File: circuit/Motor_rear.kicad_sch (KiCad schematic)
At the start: 42 parts, among them J15 motor1, J16 motor1, Q13 DMHT6016LFJ, Q14 DMHT6016LFJ, Q19 DMN1054UCB4, Q20 DMN1054UCB4, U13 SN74LVC1G18DSFR, U14 SN74LVC1G18DSFR, U15 DRV8701, U16 DRV8701

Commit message: AD変換の取得ができた
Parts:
- Q13, Q14: symbol robocon:DMHT6016LFJ -> robot_contest:DMHT6016LFJ
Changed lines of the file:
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@@
 	)
 	(symbol
-		(lib_id "robocon:DMHT6016LFJ")
+		(lib_id "robot_contest:DMHT6016LFJ")
 		(at 209.55 55.88 90)
 		(unit 1)
@@
 	)
 	(symbol
-		(lib_name "DMHT6016LFJ_1")
-		(lib_id "robocon:DMHT6016LFJ")
+		(lib_id "robot_contest:DMHT6016LFJ")
 		(at 209.55 133.35 90)
 		(unit 1)

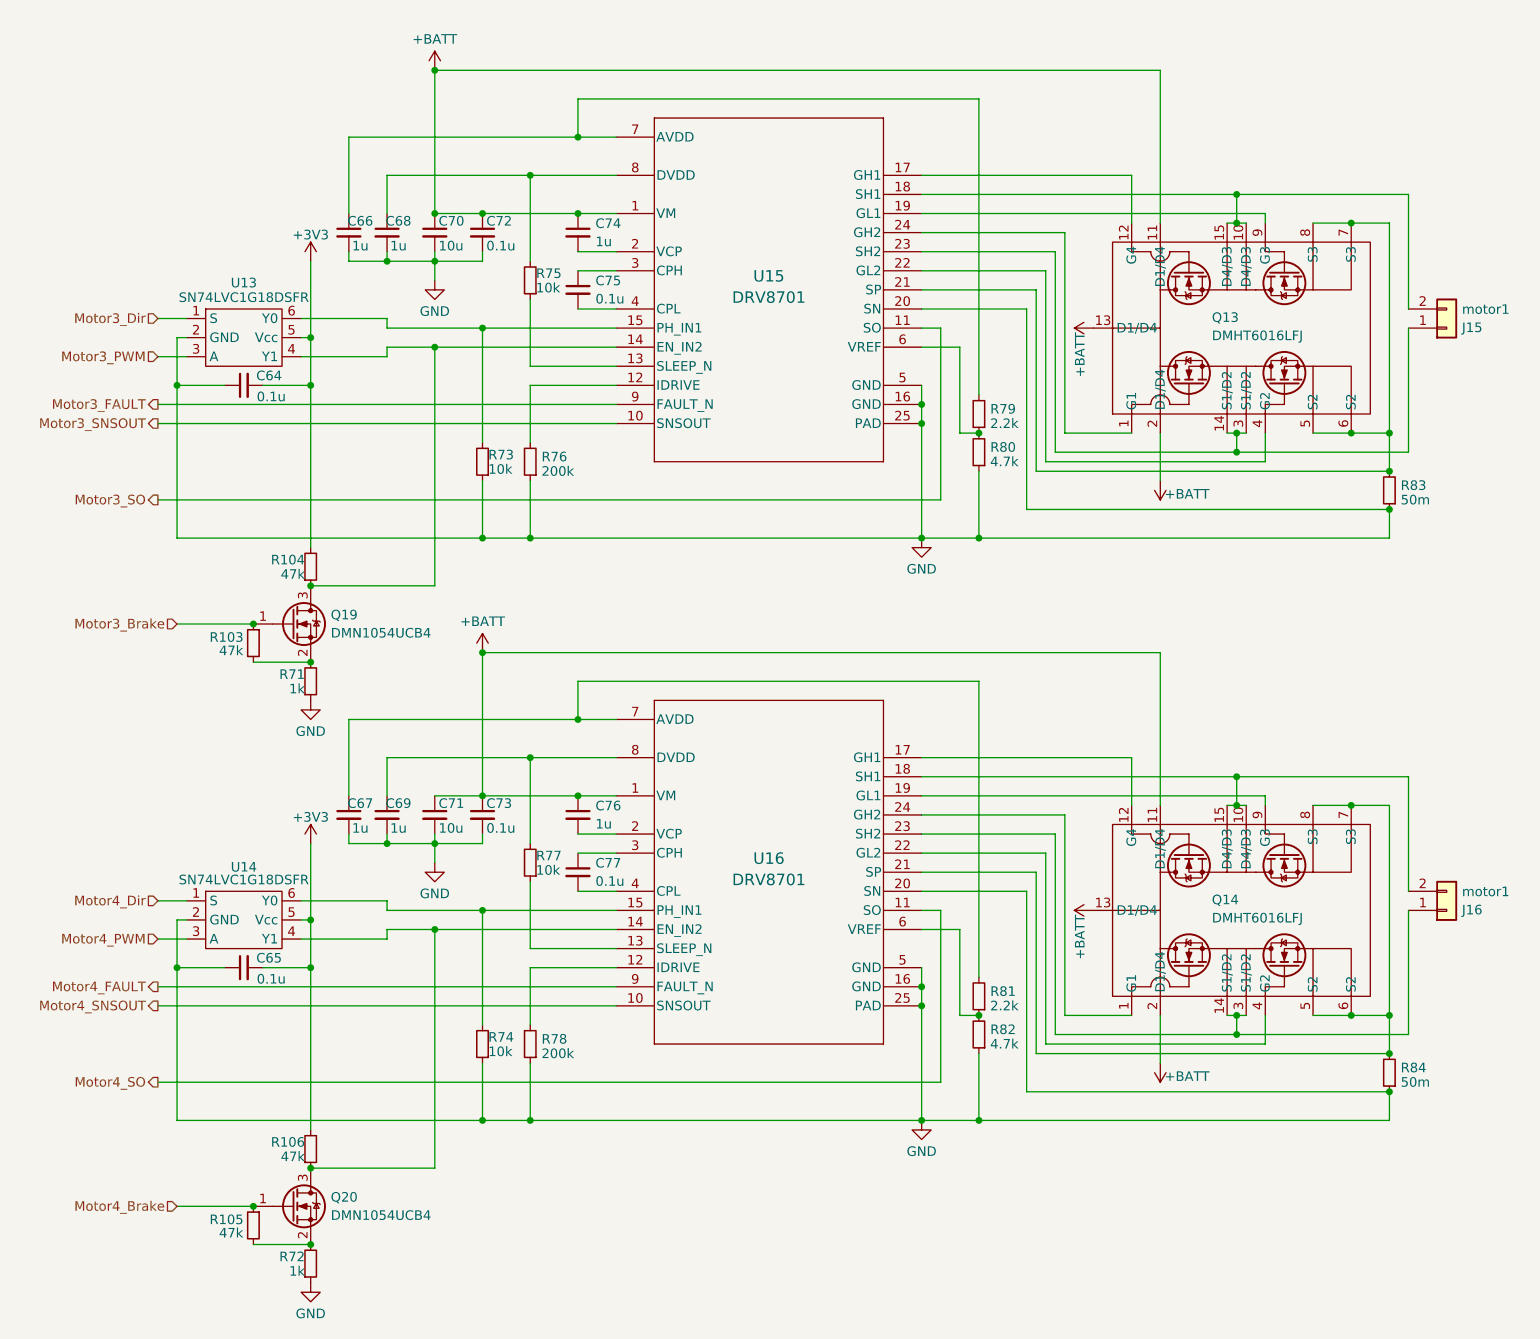
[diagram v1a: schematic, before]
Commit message: スマコンの設定変更 回路図変更
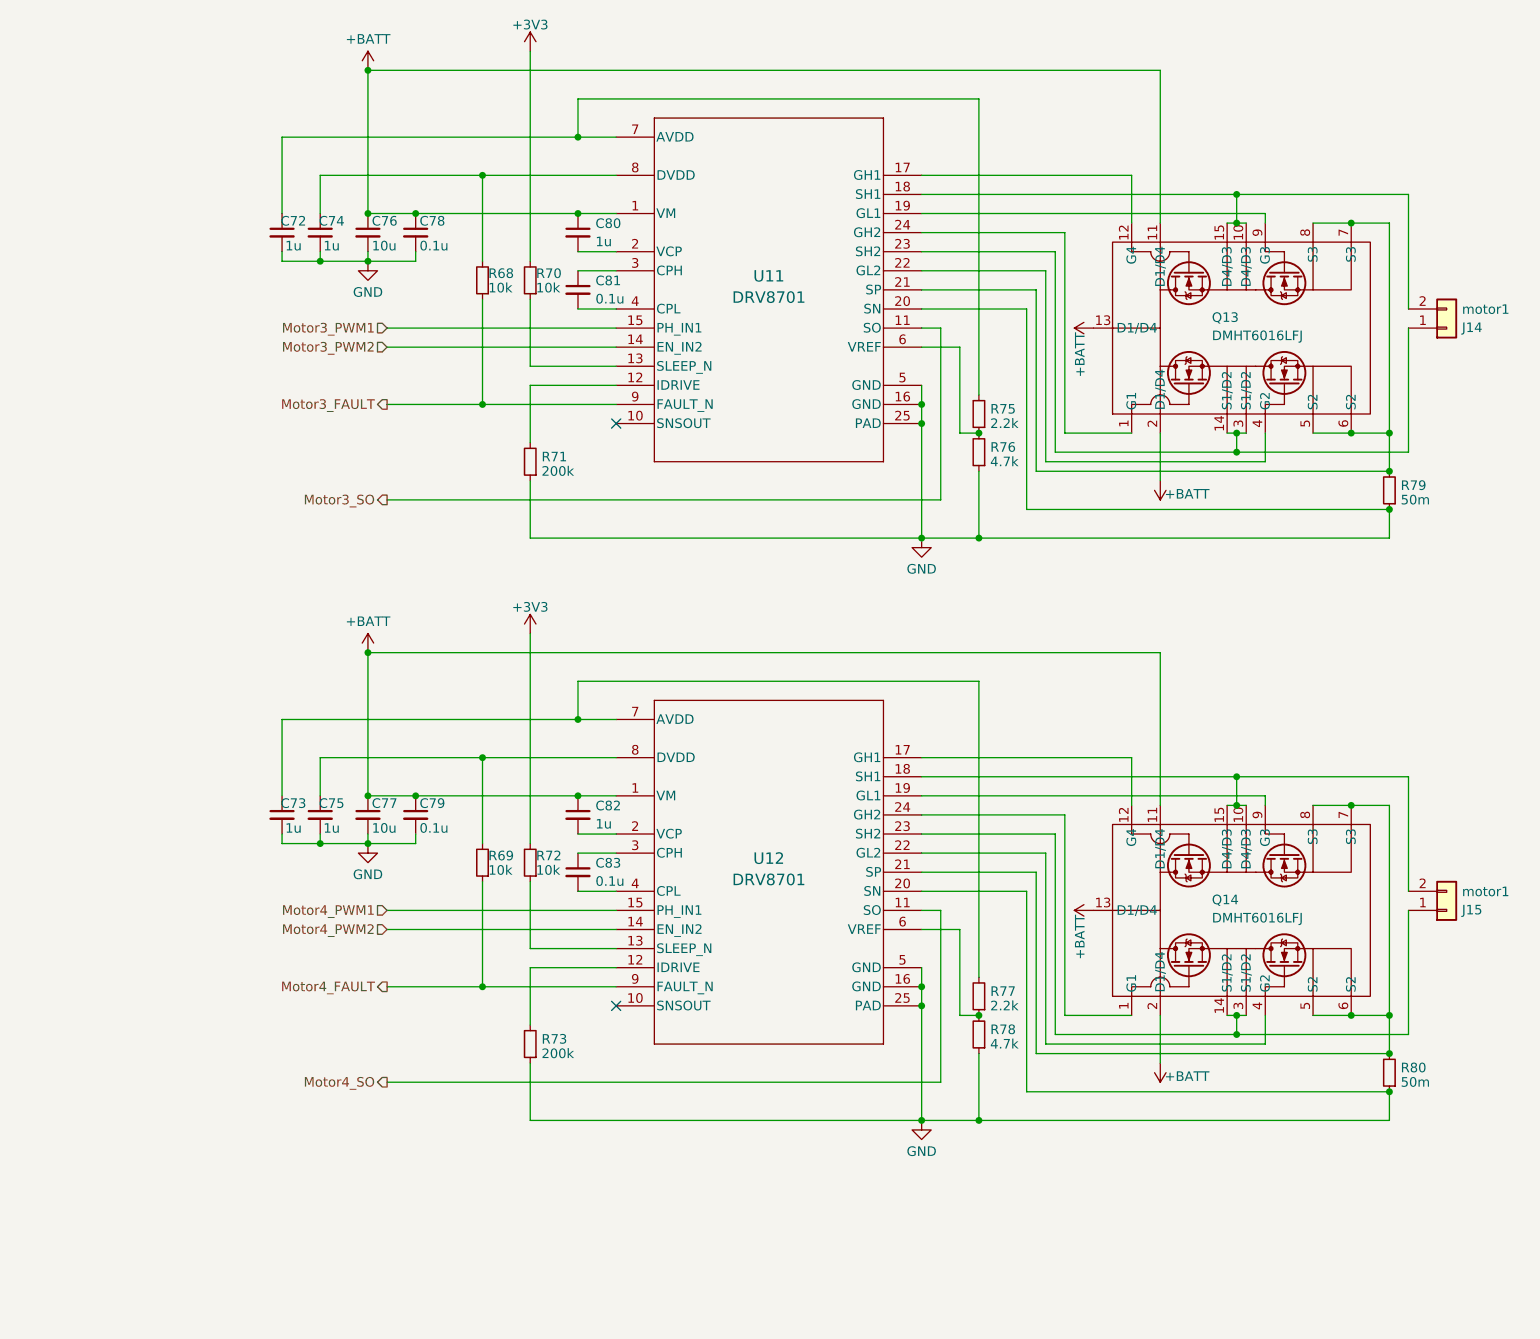
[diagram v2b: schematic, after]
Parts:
- removed C64, C65: 0.1u, Capacitor_SMD:C_0402_1005Metric, symbol Device:C_Small
- removed Q19, Q20: DMN1054UCB4, robot_contest:DMN1054UCB4, symbol Device:Q_NMOS_GSD
- removed R103, R104, R105, R106: 47k, Resistor_SMD:R_0402_1005Metric, symbol Device:R_Small
- removed R71, R72: 1k, Resistor_SMD:R_0402_1005Metric, symbol Device:R_Small
- removed R73, R74: 10k, Resistor_SMD:R_0402_1005Metric, symbol Device:R_Small
- removed U13, U14: SN74LVC1G18DSFR, robot_contest:SN74LVC1G18DSFR, symbol robocon:SN74LVC1G18
- added R68, R69: 10k, Resistor_SMD:R_0402_1005Metric, symbol Device:R_Small
- U11: renamed from U15; symbol robocon:DRV8701 -> robot_contest:DRV8701
- U12: renamed from U16; symbol robocon:DRV8701 -> robot_contest:DRV8701
- renumbered C66 to C72, C67 to C73, C68 to C74, C69 to C75, C70 to C76, C71 to C77, C72 to C78, C73 to C79, C74 to C80, C75 to C81, C76 to C82, C77 to C83, J15 to J14, J16 to J15, R75 to R70, R76 to R71, R77 to R72, R78 to R73, R79 to R75, R80 to R76, R81 to R77, R82 to R78, R83 to R79, R84 to R80
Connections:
- net +3V3: now also R70.2, R72.2
- net Motor3_FAULT: now also R68.1
- net Motor4_FAULT: now also R69.1
- net at C75.1, U12.8 (DVDD): now also R69.2; no longer R72.2
- net Motor4_PWM2: now reaches U12.14 (EN_IN2)
- net at C74.1, U11.8 (DVDD): now also R68.2; no longer R70.2
- net Motor3_PWM2: now reaches U11.14 (EN_IN2)
- net Motor3_PWM1: now reaches U11.15 (PH_IN1)
- net Motor4_PWM1: now reaches U12.15 (PH_IN1)
- net Motor3_SNSOUT: no longer names the net of U11.10 (SNSOUT)
- net Motor4_SNSOUT: no longer names the net of U12.10 (SNSOUT)
- no-connect marks 0 -> 2
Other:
- moved on the sheet: C72, C73, C74, C75, C76, C77, C78, C79
